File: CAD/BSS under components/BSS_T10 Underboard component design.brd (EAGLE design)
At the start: 23.3 x 22.8 mm, 9 parts, among them IC1 7805DT

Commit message: Board labels
Improved labeling of board
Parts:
- TO_SEN, VOLT_IN: value (none) -> MA03-1
- renumbered CBP1 to C3, LED1 to LED
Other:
- board text removed: ".1uF"
- board text removed: "1k"

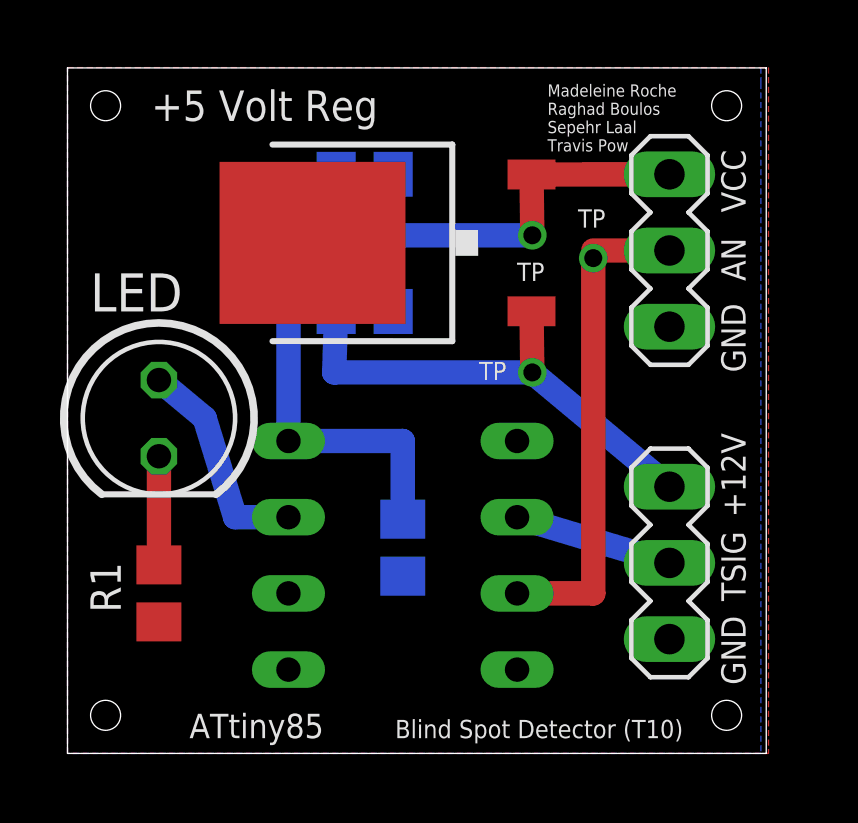
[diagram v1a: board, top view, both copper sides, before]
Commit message: Different Pins
Changed pins to AVR
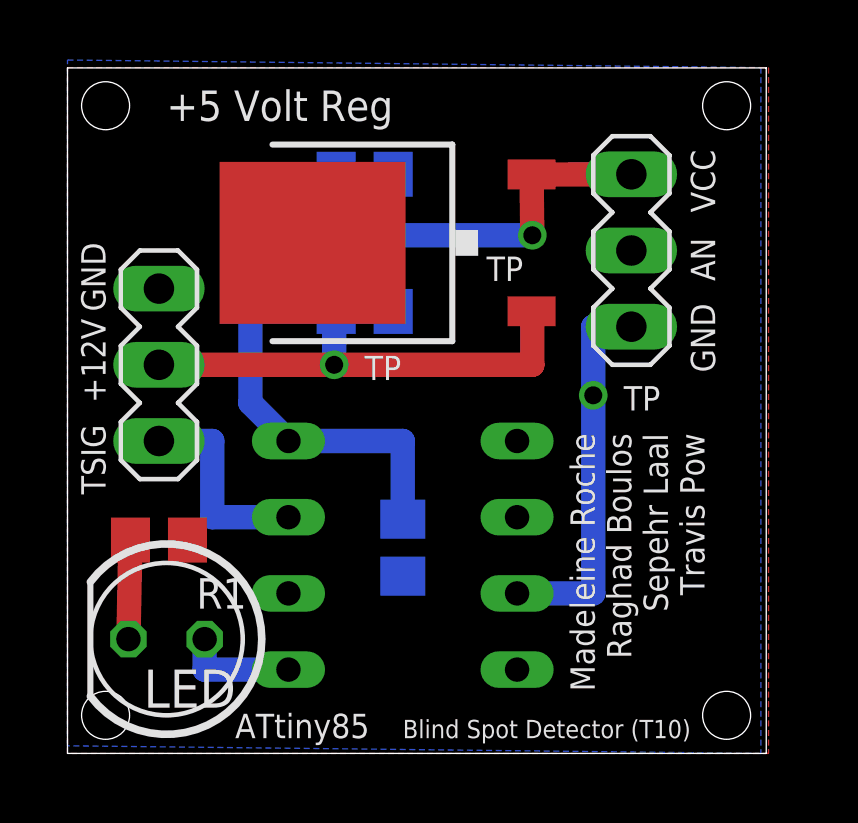
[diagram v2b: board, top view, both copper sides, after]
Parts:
- moved VOLT_IN 18.3 mm to (50.3, 48.5), turned to 270 degrees
- moved LED 7.37 mm to (50.5, 39.4), turned to 180 degrees
- moved R1 1.78 mm to (50.3, 42.7), turned to 180 degrees
- moved TO_SEN 1.27 mm to (66.0, 52.3)
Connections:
- removed net AN: AVR.3, TO_SEN.2
- new net N$1: AVR.3, TO_SEN.1
- net 12VBATTERY: now also VOLT_IN.2; no longer VOLT_IN.3
- net GND: now also TO_SEN.2; no longer TO_SEN.1
- net N$4: now also AVR.5; no longer AVR.7
- net TSIG: now also AVR.7, VOLT_IN.3; no longer AVR.2, VOLT_IN.2
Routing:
- net AN: track 16.5 -> 0.00 mm, vias 1 -> 0
- net N$1: track 0.00 -> 12.7 mm, vias 0 -> 1
- net N$4: track 7.22 -> 3.81 mm
- net +5V: track 31.6 -> 33.4 mm
- net TSIG: track 5.30 -> 6.86 mm
- net 12VBATTERY: track 16.6 -> 16.1 mm
